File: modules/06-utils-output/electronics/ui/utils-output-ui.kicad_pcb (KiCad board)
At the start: 2 copper layers, 58 x 110 mm, 36 parts, among them J1 Conn_02x03_Odd_Even, J2 Conn_02x04_Odd_Even, J4 Conn_01x02, J5 Conn_01x06, J6 Conn_02x05_Odd_Even, J7 Conn_02x03_Odd_Even, Q1 2N3904, Q2 2N3906

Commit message: Re-exported all UI board production files after fixing pot bug
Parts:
- RV_LFO_RATE1: value A500k -> A500k-1M
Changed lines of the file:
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@@
 			)
 		)
-		(property "Part URL" ""
+		(property "Part URL" "https://mou.sr/4a8lju1"
 			(at 0 0 90)
 			(unlocked yes)
@@
 			)
 		)
-		(property "Vendor" ""
+		(property "Vendor" "Mouser"
 			(at 0 0 90)
 			(unlocked yes)
@@
 			)
 		)
+		(property "Part no." "637-2N3906"
+			(at 0 0 90)
+			(unlocked yes)
+			(layer "F.Fab")
+			(hide yes)
+			(effects
+				(font
+					(size 1 1)
+					(thickness 0.15)
+				)
+			)
+		)
 		(property ki_fp_filters "TO?92*")
 		(sheetname "/")
@@
 			)
 		)
-		(property "Value" "A500k"
+		(property "Value" "A500k-1M"
 			(at 0.1 13.379024 180)
 			(layer "F.Fab")
@@
 			)
 		)
-		(property "Part URL" "https://mou.sr/4694GMU"
+		(property "Part URL" "https://mou.sr/3VpxrOs"
 			(at 0 0 0)
 			(unlocked yes)
@@
 			)
 		)
-		(property "Part no." "652-PTV09A4025FB104"
+		(property "Part no." "652-PTV09A4025FA105"
 			(at 0 0 0)
 			(unlocked yes)
@@
 			)
 		)
-		(property "Part URL" ""
+		(property "Part URL" "https://mou.sr/4febysZ"
 			(at 0 0 0)
 			(unlocked yes)
@@
 			)
 		)
-		(property "Vendor" ""
+		(property "Vendor" "Mouser"
 			(at 0 0 0)
 			(unlocked yes)
@@
 			)
 		)
+		(property "Part no." "637-2N3904"
+			(at 0 0 0)
+			(unlocked yes)
+			(layer "F.Fab")
+			(hide yes)
+			(effects
+				(font
+					(size 1 1)
+					(thickness 0.15)
+				)
+			)
+		)
 		(property ki_fp_filters "TO?92*")
 		(sheetname "/")
@@
 			)
 		)
-		(property "Part URL" "https://mou.sr/4694GMU"
+		(property "Part URL" "https://mou.sr/3VpxrOs"
 			(at 0 0 0)
 			(unlocked yes)
@@
 			)
 		)
-		(property "Part no." "652-PTV09A4025FB104"
+		(property "Part no." "652-PTV09A4025FA105"
 			(at 0 0 0)
 			(unlocked yes)
@@
 			)
 		)
-		(property "Part URL" "https://mou.sr/4694GMU"
+		(property "Part URL" "https://mou.sr/4bCOV0e"
 			(at 0 0 0)
 			(unlocked yes)
@@
 			)
 		)
-		(property "Part no." "652-PTV09A4025FB104"
+		(property "Part no." "652-PTV09A4025FA103"
 			(at 0 0 0)
 			(unlocked yes)
@@
 			)
 		)
-		(property "Vendor" ""
+		(property "Vendor" "Mouser"
 			(at 0 0 0)
 			(unlocked yes)
@@
 			)
 		)
+		(property "Part no." "652-PTV1124425AA203 "
+			(at 0 0 0)
+			(unlocked yes)
+			(layer "F.Fab")
+			(hide yes)
+			(effects
+				(font
+					(size 1 1)
+					(thickness 0.15)
+				)
+			)
+		)
 		(property ki_fp_filters "Potentiometer*")
 		(sheetname "/")
@@
 			)
 		)
-		(property "Part URL" ""
+		(property "Part URL" "https://mou.sr/4q072Ei"
 			(at 0 0 270)
 			(unlocked yes)
@@
 			)
 		)
-		(property "Vendor" ""
+		(property "Vendor" "Mouser"
 			(at 0 0 270)
 			(unlocked yes)
@@
 			)
 		)
+		(property "Part no." "603-MFR25SFTF52-4K7"
+			(at 0 0 270)
+			(unlocked yes)
+			(layer "F.Fab")
+			(hide yes)
+			(effects
+				(font
+					(size 1 1)
+					(thickness 0.15)
+				)
+			)
+		)
 		(property ki_fp_filters "R_*")
 		(sheetname "/")
@@
 			)
 		)
-		(property "Part URL" ""
+		(property "Part URL" "https://mou.sr/3MWzgkZ"
 			(at 0 0 180)
 			(unlocked yes)
@@
 			)
 		)
-		(property "Vendor" ""
+		(property "Vendor" "Mouser"
 			(at 0 0 180)
 			(unlocked yes)
@@
 			)
 		)
+		(property "Part no." "603-MFR-25FRF52-47K"
+			(at 0 0 180)
+			(unlocked yes)
+			(layer "F.Fab")
+			(hide yes)
+			(effects
+				(font
+					(size 1 1)
+					(thickness 0.15)
+				)
+			)
+		)
 		(property ki_fp_filters "R_*")
 		(sheetname "/")
@@
 			)
 		)
-		(property "Part URL" ""
+		(property "Part URL" "https://mou.sr/4qqxl75"
 			(at 0 0 270)
 			(unlocked yes)
@@
 			)
 		)
-		(property "Vendor" ""
+		(property "Vendor" "Mouser"
 			(at 0 0 270)
 			(unlocked yes)
@@
 			)
 		)
+		(property "Part no." "200-SSW10401TD"
+			(at 0 0 90)
+			(unlocked yes)
+			(layer "B.Fab")
+			(hide yes)
+			(effects
+				(font
+					(size 1 1)
+					(thickness 0.15)
+				)
+				(justify mirror)
+			)
+		)
 		(property ki_fp_filters "Connector*:*_2x??_*")
 		(sheetname "/")
@@
 			)
 		)
-		(property "Part URL" ""
+		(property "Part URL" "https://mou.sr/4lVCZM9"
 			(at 0 0 90)
 			(unlocked yes)
@@
 			)
 		)
-		(property "Vendor" ""
+		(property "Vendor" "Mouser"
 			(at 0 0 90)
 			(unlocked yes)
@@
 			)
 		)
+		(property "Part no." "200-SSW10501TD"
+			(at 0 0 270)
+			(unlocked yes)
+			(layer "B.Fab")
+			(hide yes)
+			(effects
+				(font
+					(size 1 1)
+					(thickness 0.15)
+				)
+				(justify mirror)
+			)
+		)
 		(property ki_fp_filters "Connector*:*_2x??_*")
 		(sheetname "/")
@@
 			)
 		)
-		(property "Part URL" ""
+		(property "Part URL" "https://mou.sr/3GIDVEr"
 			(at 0 0 90)
 			(unlocked yes)
@@
 			)
 		)
-		(property "Vendor" ""
+		(property "Vendor" "Mouser"
 			(at 0 0 90)
 			(unlocked yes)
@@
 			(unlocked yes)
 			(layer "B.Fab")
+			(hide yes)
+			(effects
+				(font
+					(size 1 1)
+					(thickness 0.15)
+				)
+				(justify mirror)
+			)
+		)
+		(property "Part no." "200-SSW10301TD"
+			(at 0 0 270)
+			(unlocked yes)
+			(layer "B.Fab")

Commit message: Re-generated all production files
Nothing changed, but regenerated production files for next batch order.
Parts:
- J_MAIN_OUT1: value PJ398SM -> PJ366ST
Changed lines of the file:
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@@
 			)
 		)
-		(property "Value" "PJ398SM"
+		(property "Value" "PJ366ST"
 			(at 0 -1.48 180)
 			(layer "F.Fab")

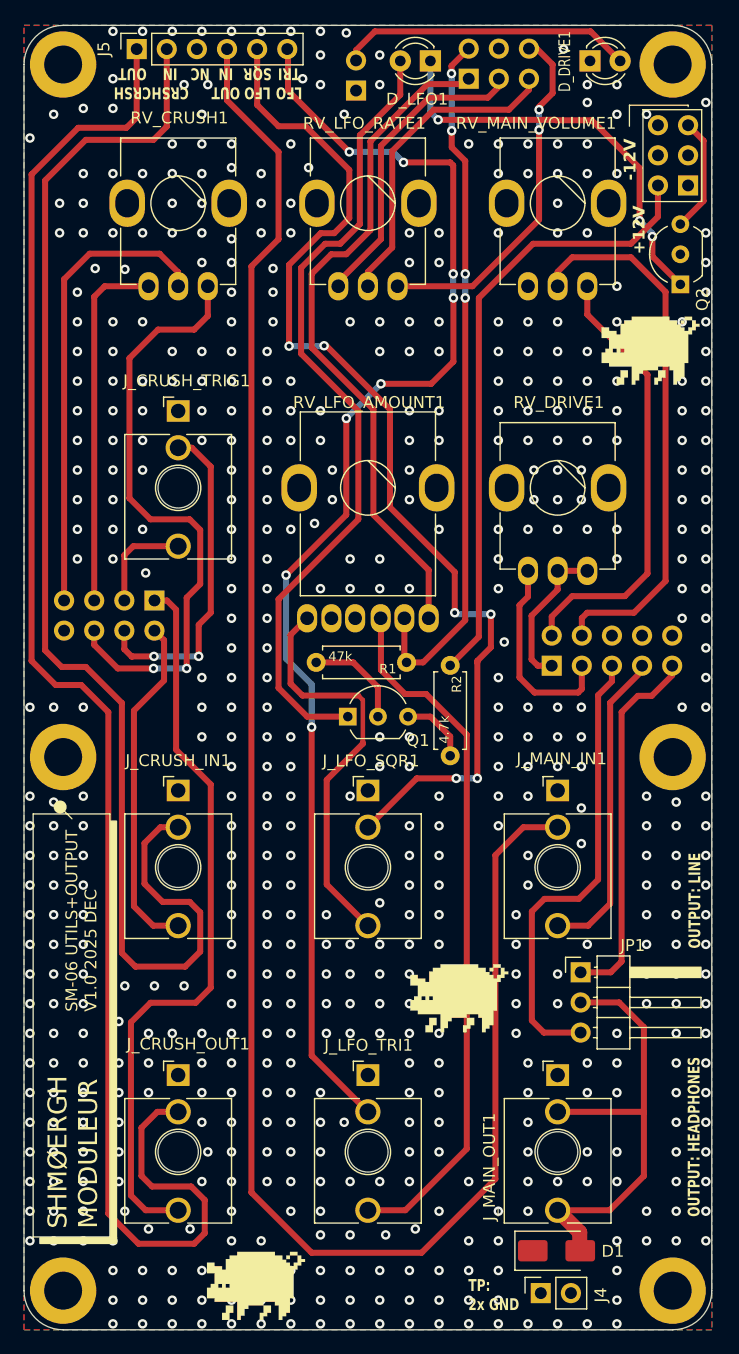
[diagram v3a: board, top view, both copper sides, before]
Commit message: Improved LFO LED network
The LFO LED transistor needed a little feedback bias to make it pulse nicely along with the triangle wave.
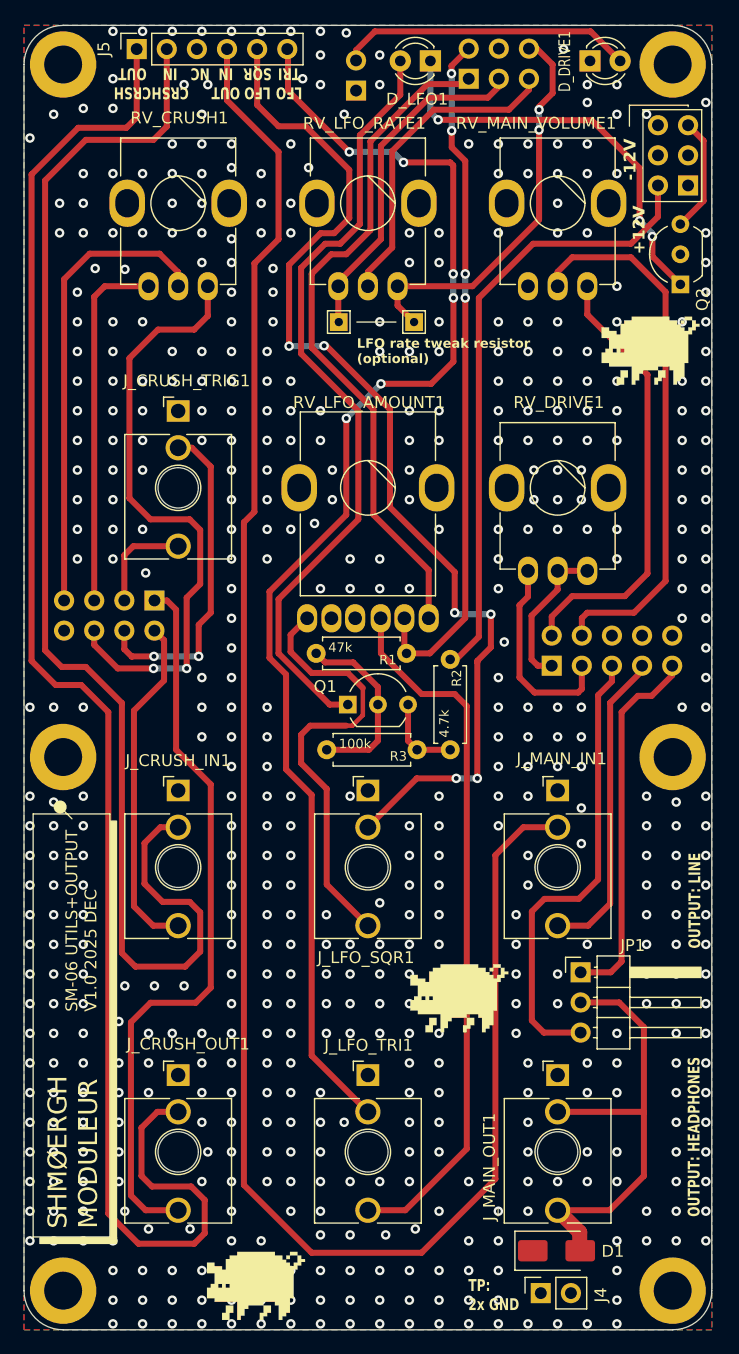
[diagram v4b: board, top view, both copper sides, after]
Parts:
- added J3: Conn_01x01_Pin, TestPoint:TestPoint_THTPad_1.5x1.5mm_Drill0.7mm, F.Cu at (156.9, 69.0)
- added J8: Conn_01x01_Pin, TestPoint:TestPoint_THTPad_1.5x1.5mm_Drill0.7mm, F.Cu at (150.5, 69.0)
- added R3: 100k, Shmoergh_Custom_Footprints:R_Axial_DIN0207_L6.3mm_D2.5mm_P7.62mm_Horizontal, F.Cu at (157.1, 105.1)
- moved Q1 1.02 mm to (151.3, 101.3)
- moved R1 0.76 mm to (156.3, 97.0)
- moved R2 0.51 mm to (159.9, 97.5)
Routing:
- net Net-(Q1-B): track 8.56 -> 15.5 mm
- net LFO_POT_3: track 30.4 -> 34.0 mm
- net LFO_POT_1: track 26.0 -> 29.0 mm
- net Net-(J_LFO_SQR1-PadT): track 34.5 -> 37.4 mm
- net Net-(D_LFO1-A): track 68.7 -> 66.6 mm
- net LFO_TRI: track 59.5 -> 58.3 mm
- net LFO_TRI_DEFAULT: track 111.1 -> 112.2 mm, vias 8 -> 6
- net Net-(Q1-C): track 5.88 -> 6.92 mm
- net Net-(J_LFO_TRI1-PadT): track 59.3 -> 59.9 mm
- net OUTPUT_IN_DEFAULT: track 158.0 -> 158.5 mm
- net GND: vias 565 -> 553
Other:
- board text added: "LFO rate tweak resistor (optional)"

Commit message: Updated version number of Utils UI board
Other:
- board text added: "SM-06 UTILS+OUTPUT V1.1 2026 JAN"
- board text removed: "SM-06 UTILS+OUTPUT V1.0 2025 DEC"
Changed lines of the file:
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@@
 		)
 	)
-	(gr_text "SM-06 UTILS+OUTPUT\nV1.0 2025 DEC"
+	(gr_text "SM-06 UTILS+OUTPUT\nV1.1 2026 JAN"
 		(at 130.223 127.185 90)
 		(layer "F.SilkS")
@@
 			(justify left bottom)
 		)
-		(render_cache "SM-06 UTILS+OUTPUT\nV1.0 2025 DEC" 90
+		(render_cache "SM-06 UTILS+OUTPUT\nV1.1 2026 JAN" 90
 			(polygon
 				(pts
@@
 			(polygon
 				(pts
-					(xy 129.162124 124.387686) (xy 129.925749 124.387686) (xy 129.925749 124.260436) (xy 129.671187 124.260436)
-					(xy 129.671187 124.133124) (xy 129.543936 124.133124) (xy 129.543936 124.260436) (xy 129.162124 124.260436)
-				)
-			)
-			(polygon
-				(pts
-					(xy 129.925749 124.260436) (xy 130.053 124.260436) (xy 130.053 123.878623) (xy 129.925749 123.878623)
-				)
-			)
-			(polygon
-				(pts
-					(xy 129.034812 124.260436) (xy 129.162124 124.260436) (xy 129.162124 123.878623) (xy 129.034812 123.878623)
-				)
-			)
-			(polygon
-				(pts
-					(xy 129.162124 123.878623) (xy 129.289374 123.878623) (xy 129.289374 124.005874) (xy 129.416686 124.005874)
-					(xy 129.416686 123.878623) (xy 129.925749 123.878623) (xy 129.925749 123.751311) (xy 129.162124 123.751311)
-				)
-			)
-			(polygon
-				(pts
-					(xy 129.416686 124.133124) (xy 129.543936 124.133124) (xy 129.543936 124.005874) (xy 129.416686 124.005874)
+					(xy 129.289374 124.133124) (xy 129.925749 124.133124) (xy 129.925749 124.387686) (xy 130.053 124.387686)
+					(xy 130.053 123.751311) (xy 129.925749 123.751311) (xy 129.925749 124.005874) (xy 129.034812 124.005874)
+					(xy 129.034812 124.133124) (xy 129.162124 124.133124) (xy 129.162124 124.387686) (xy 129.289374 124.387686)
 				)
 			)
@@
 			(polygon
 				(pts
-					(xy 129.034812 119.937581) (xy 129.543936 119.937581) (xy 129.543936 119.428518) (xy 129.416686 119.428518)
-					(xy 129.416686 119.810331) (xy 129.162124 119.810331) (xy 129.162124 119.301207) (xy 129.034812 119.301207)
+					(xy 129.034812 119.810331) (xy 129.162124 119.810331) (xy 129.162124 119.428518) (xy 129.034812 119.428518)
+				)
+			)
+			(polygon
+				(pts
+					(xy 129.162124 119.937581) (xy 129.925749 119.937581) (xy 129.925749 119.810331) (xy 129.543936 119.810331)
+					(xy 129.543936 119.428518) (xy 129.416686 119.428518) (xy 129.416686 119.810331) (xy 129.162124 119.810331)
 				)
 			)
@@
 			(polygon
 				(pts
-					(xy 129.925749 119.428518) (xy 129.925749 119.810331) (xy 130.053 119.810331) (xy 130.053 119.428518)
-				)
-			)
-			(polygon
-				(pts
-					(xy 129.925749 119.810331) (xy 129.798498 119.810331) (xy 129.798498 119.937581) (xy 129.925749 119.937581)
-				)
-			)
-			(polygon
-				(pts
-					(xy 129.034812 118.15754) (xy 130.053 118.15754) (xy 130.053 117.648476) (xy 129.925749 117.648476)
-					(xy 129.925749 118.030289) (xy 129.162124 118.030289) (xy 129.162124 117.648476) (xy 129.034812 117.648476)
-				)
-			)
-			(polygon
-				(pts
-					(xy 129.162124 117.648476) (xy 129.925749 117.648476) (xy 129.925749 117.521165) (xy 129.162124 117.521165)
-				)
-			)
-			(polygon
-				(pts
-					(xy 129.034812 117.267519) (xy 130.053 117.267519) (xy 130.053 116.631144) (xy 129.925749 116.631144)
-					(xy 129.925749 117.140268) (xy 129.543936 117.140268) (xy 129.543936 116.758456) (xy 129.416686 116.758456)
-					(xy 129.416686 117.140268) (xy 129.162124 117.140268) (xy 129.162124 116.631144) (xy 129.034812 116.631144)
-				)
-			)
-			(polygon
-				(pts
-					(xy 129.162124 116.377498) (xy 129.925749 116.377498) (xy 129.925749 116.250247) (xy 129.162124 116.250247)
-				)
-			)
-			(polygon
-				(pts
-					(xy 129.925749 116.250247) (xy 130.053 116.250247) (xy 130.053 115.868435) (xy 129.925749 115.868435)
-				)
-			)
-			(polygon
-				(pts
-					(xy 129.798498 115.868435) (xy 129.925749 115.868435) (xy 129.925749 115.741123) (xy 129.798498 115.741123)
-				)
-			)
-			(polygon
-				(pts
-					(xy 129.034812 116.250247) (xy 129.162124 116.250247) (xy 129.162124 115.868435) (xy 129.034812 115.868435)
-				)
-			)
-			(polygon
-				(pts
-					(xy 129.162124 115.868435) (xy 129.289374 115.868435) (xy 129.289374 115.741123) (xy 129.162124 115.741123)
-				)
-			)
+					(xy 129.925749 119.810331) (xy 130.053 119.810331) (xy 130.053 119.428518) (xy 129.925749 119.428518)
+				)
+			)
+			(polygon
+				(pts
+					(xy 129.162124 119.428518) (xy 129.289374 119.428518) (xy 129.289374 119.301207) (xy 129.162124 119.301207)
+				)
+			)
+			(polygon
+				(pts
+					(xy 129.925749 118.030289) (xy 129.798498 118.030289) (xy 129.798498 118.15754) (xy 129.925749 118.15754)
+				)
+			)
+			(polygon
+				(pts
+					(xy 129.925749 118.030289) (xy 130.053 118.030289) (xy 130.053 117.648476) (xy 129.925749 117.648476)
+				)
+			)
+			(polygon
+				(pts
+					(xy 129.162124 117.648476) (xy 129.925749 117.648476) (xy 129.925749 117.521165) (xy 129.034812 117.521165)
+					(xy 129.034812 117.902978) (xy 129.162124 117.902978)
+				)
+			)
+			(polygon
+				(pts
+					(xy 129.289374 117.267519) (xy 130.053 117.267519) (xy 130.053 117.140268) (xy 129.671187 117.140268)
+					(xy 129.671187 116.758456) (xy 130.053 116.758456) (xy 130.053 116.631144) (xy 129.289374 116.631144)
+					(xy 129.289374 116.758456) (xy 129.543936 116.758456) (xy 129.543936 117.140268) (xy 129.289374 117.140268)
+				)
+			)
+			(polygon
+				(pts
+					(xy 129.034812 117.012957) (xy 129.162124 117.012957) (xy 129.162124 116.885706) (xy 129.034812 116.885706)
+				)
+			)
+			(polygon
+				(pts
+					(xy 129.162124 117.140268) (xy 129.289374 117.140268) (xy 129.289374 117.012957) (xy 129.162124 117.012957)
+				)
+			)
+			(polygon
+				(pts
+					(xy 129.162124 116.885706) (xy 129.289374 116.885706) (xy 129.289374 116.758456) (xy 129.162124 116.758456)
+				)
+			)
+			(polygon
+				(pts
+					(xy 129.034812 116.377498) (xy 130.053 116.377498) (xy 130.053 116.250247) (xy 129.416686 116.250247)
+					(xy 129.416686 116.122936) (xy 129.289374 116.122936) (xy 129.289374 116.250247) (xy 129.034812 116.250247)
+				)
+			)
+			(polygon
+				(pts
+					(xy 129.671187 115.868435) (xy 130.053 115.868435) (xy 130.053 115.741123) (xy 129.034812 115.741123)
+					(xy 129.034812 115.868435) (xy 129.543936 115.868435) (xy 129.543936 115.995685) (xy 129.671187 115.995685)
+				)
+			)
+			(polygon
+				(pts
+					(xy 129.543936 115.995685) (xy 129.416686 115.995685) (xy 129.416686 116.122936) (xy 129.543936 116.122936)
+				)
+			)

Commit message: Added protection resistor to pulse out on Brain
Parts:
- J3, J8: footprint TestPoint:TestPoint_THTPad_1.5x1.5mm_Drill0.7mm -> TestPoint:TestPoint_THTPad_D2.0mm_Drill1.0mm
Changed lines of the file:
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@@
 		(embedded_fonts no)
 	)
-	(footprint "TestPoint:TestPoint_THTPad_1.5x1.5mm_Drill0.7mm"
+	(footprint "TestPoint:TestPoint_THTPad_D2.0mm_Drill1.0mm"
 		(layer "F.Cu")
 		(at 150.543 69.019)
-		(descr "THT rectangular pad as test Point, square 1.5mm side length, hole diameter 0.7mm")
-		(tags "test point THT pad rectangle square")
+		(descr "THT pad as test Point, diameter 2.0mm, hole diameter 1.0mm")
+		(tags "test point THT pad")
 		(property "Reference" "J8"
-			(at -0.127 2.159 0)
+			(at 0 -1.998 0)
 			(layer "User.1")
 			(effects
@@
 		)
 		(property "Value" "Conn_01x01_Pin"
-			(at 0 1.75 0)
+			(at 0 2.05 0)
 			(layer "F.Fab")
 			(effects
@@
 		(sheetfile "utils-output-ui.kicad_sch")
 		(attr exclude_from_pos_files)
-		(fp_line
-			(start -0.95 -0.95)
-			(end 0.95 -0.95)
-			(stroke
-				(width 0.12)
-				(type solid)
-			)
-			(layer "F.SilkS")
-		)
-		(fp_line
-			(start -0.95 0.95)
-			(end -0.95 -0.95)
-			(stroke
-				(width 0.12)
-				(type solid)
-			)
-			(layer "F.SilkS")
-		)
-		(fp_line
-			(start 0.95 -0.95)
-			(end 0.95 0.95)
-			(stroke
-				(width 0.12)
-				(type solid)
-			)
-			(layer "F.SilkS")
-		)
-		(fp_line
-			(start 0.95 0.95)
-			(end -0.95 0.95)
+		(fp_circle
+			(center 0 0)
+			(end 0 1.2)
 			(stroke
 				(width 0.12)
 				(type solid)
 			)
+			(fill no)
 			(layer "F.SilkS")
 		)
-		(fp_line
-			(start -1.25 -1.25)
-			(end -1.25 1.25)
-			(stroke
-				(width 0.05)
-				(type solid)
-			)
-			(layer "F.CrtYd")
-		)
-		(fp_line
-			(start -1.25 -1.25)
-			(end 1.25 -1.25)
-			(stroke
-				(width 0.05)
-				(type solid)
-			)
-			(layer "F.CrtYd")
-		)
-		(fp_line
-			(start 1.25 1.25)
-			(end -1.25 1.25)
-			(stroke
-				(width 0.05)
-				(type solid)
-			)
-			(layer "F.CrtYd")
-		)
-		(fp_line
-			(start 1.25 1.25)
-			(end 1.25 -1.25)
+		(fp_circle
+			(center 0 0)
+			(end 1.5 0)
 			(stroke
 				(width 0.05)
 				(type solid)
 			)
+			(fill no)
 			(layer "F.CrtYd")
 		)
 		(fp_text user "${REFERENCE}"
-			(at 0 -1.65 0)
+			(at 0 -2 0)
 			(layer "F.Fab")
 			(effects
@@
 			)
 		)
-		(pad "1" thru_hole rect
+		(pad "1" thru_hole circle
 			(at 0 0)
-			(size 1.5 1.5)
-			(drill 0.7)
+			(size 2 2)
+			(drill 1)
 			(layers "*.Cu" "*.Mask")
 			(remove_unused_layers no)
@@
 		(embedded_fonts no)
 	)
-	(footprint "TestPoint:TestPoint_THTPad_1.5x1.5mm_Drill0.7mm"
+	(footprint "TestPoint:TestPoint_THTPad_D2.0mm_Drill1.0mm"
 		(layer "F.Cu")
 		(at 156.893 69.019)
-		(descr "THT rectangular pad as test Point, square 1.5mm side length, hole diameter 0.7mm")
-		(tags "test point THT pad rectangle square")
+		(descr "THT pad as test Point, diameter 2.0mm, hole diameter 1.0mm")
+		(tags "test point THT pad")
 		(property "Reference" "J3"
-			(at 0 -1.648 0)
+			(at 0 -1.998 0)
 			(layer "User.1")
 			(effects
@@
 		)
 		(property "Value" "Conn_01x01_Pin"
-			(at 0 1.75 0)
+			(at 0 2.05 0)
 			(layer "F.Fab")
 			(effects
@@
 		(sheetfile "utils-output-ui.kicad_sch")
 		(attr exclude_from_pos_files)
-		(fp_line
-			(start -0.95 -0.95)
-			(end 0.95 -0.95)
-			(stroke
-				(width 0.12)
-				(type solid)
-			)
-			(layer "F.SilkS")
-		)
-		(fp_line
-			(start -0.95 0.95)
-			(end -0.95 -0.95)
-			(stroke
-				(width 0.12)
-				(type solid)
-			)
-			(layer "F.SilkS")
-		)
-		(fp_line
-			(start 0.95 -0.95)
-			(end 0.95 0.95)
-			(stroke
-				(width 0.12)
-				(type solid)
-			)
-			(layer "F.SilkS")
-		)
-		(fp_line
-			(start 0.95 0.95)
-			(end -0.95 0.95)
+		(fp_circle
+			(center 0 0)
+			(end 0 1.2)
 			(stroke
 				(width 0.12)
 				(type solid)
 			)
+			(fill no)
 			(layer "F.SilkS")
 		)
-		(fp_line
-			(start -1.25 -1.25)
-			(end -1.25 1.25)
-			(stroke
-				(width 0.05)
-				(type solid)
-			)
-			(layer "F.CrtYd")
-		)
-		(fp_line
-			(start -1.25 -1.25)
-			(end 1.25 -1.25)
-			(stroke
-				(width 0.05)
-				(type solid)
-			)
-			(layer "F.CrtYd")
-		)
-		(fp_line
-			(start 1.25 1.25)
-			(end -1.25 1.25)
-			(stroke
-				(width 0.05)
-				(type solid)
-			)
-			(layer "F.CrtYd")
-		)
-		(fp_line
-			(start 1.25 1.25)
-			(end 1.25 -1.25)
+		(fp_circle
+			(center 0 0)
+			(end 1.5 0)
 			(stroke
 				(width 0.05)
 				(type solid)
 			)
+			(fill no)
 			(layer "F.CrtYd")
 		)
 		(fp_text user "${REFERENCE}"
-			(at 0 -1.65 0)
+			(at 0 -2 0)
 			(layer "F.Fab")
 			(effects
@@
 			)
 		)
-		(pad "1" thru_hole rect
+		(pad "1" thru_hole circle
 			(at 0 0)
-			(size 1.5 1.5)
-			(drill 0.7)
+			(size 2 2)
+			(drill 1)
 			(layers "*.Cu" "*.Mask")
 			(remove_unused_layers no)
@@
 	)
 	(gr_text "LFO rate tweak resistor\n(optional)"
-		(at 152.067 72.575 0)
+		(at 152.067 73.21 0)
 		(layer "F.SilkS")
 		(effects
